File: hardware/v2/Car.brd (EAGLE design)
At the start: 84 x 56 mm, 63 parts

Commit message: Completed Rev.A of v2 hardware.
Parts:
- removed 3.3V: 317EMP, linear:SOT223
- removed ARMS1: MCP23S08, microchip:SO-18W
- removed DIO1: (no value), SparkFun-Connectors:1X10_LOCK
- removed LED1, LED2: (no value), led:CHIP-LED0805
- removed POW: (no value), SparkFun-Connectors:1X02_XTRA_BIG
- added 3V3: 317EMP, linear:SOT223
- added AIO: (no value), SparkFun-Connectors:1X10_LOCK
- added HB, PWR: (no value), led:CHIP-LED0805
- added J1: (no value), con-jack:DCJ0303
- added M.ARMS: MCP23S08, microchip:SO-18W
- moved C2 28.6 mm to (48.3, 23.5), turned to 270 degrees
- moved R14 10.6 mm to (20.3, 39.4), turned to 270 degrees
- moved 5V 9.04 mm to (14.6, 38.1), turned to 180 degrees
- moved C11 8.95 mm to (8.89, 35.6), turned to 90 degrees
- moved R16 7.87 mm to (20.3, 28.6), turned to 270 degrees
- moved C12 7.33 mm to (5.08, 35.6), turned to 90 degrees
- moved R13 5.10 mm to (20.3, 34.3), turned to 270 degrees
- moved R15 4.57 mm to (20.3, 23.5), turned to 270 degrees
- moved C10 4.35 mm to (8.89, 29.2), turned to 270 degrees
- moved C5 3.58 mm to (64.8, 31.1), turned to 90 degrees
- moved RL1 3.54 mm to (5.08, 24.1), turned to 90 degrees
- moved C7 3.26 mm to (60.3, 17.1), turned to 180 degrees
- moved 22RS 3.16 mm to (28.6, 8.89)
- moved 21RS 3.12 mm to (34.3, 8.89)
- moved 12RS 3.04 mm to (28.6, 47.0)
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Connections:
- net +12V: now also 3V3.3, J1.2; no longer 3.3V.3, POW.1
- net +3V3: now also 3V3.4, AIO.1, M.ARMS.18, M.ARMS.4, M.ARMS.5; no longer 3.3V.4, ARMS1.18, ARMS1.4, ARMS1.5, DIO1.1
- net +5V: now also PWR.A; no longer LED2.A
- net GND: now also AIO.10, J1.1, M.ARMS.9; no longer ARMS1.9, DIO1.10, POW.2
- net N$20: now also 3V3.1; no longer 3.3V.1
- net N$23: now also M.ARMS.12; no longer ARMS1.12
- net N$25: now also M.ARMS.2; no longer ARMS1.2
- net N$26: now also M.ARMS.3; no longer ARMS1.3
- net N$29: now also AIO.4; no longer DIO1.4
- net N$32: now also AIO.5; no longer DIO1.5
- net N$36: now also M.ARMS.7; no longer ARMS1.7
- net N$45: now also AIO.2, HB.A; no longer DIO1.2, LED1.A
- net N$46: now also HB.C; no longer LED1.C
- net N$53: now also AIO.3; no longer DIO1.3
- net N$54: now also AIO.7; no longer DIO1.7
- net N$55: now also AIO.8; no longer DIO1.8
- net N$56: now also M.ARMS.13; no longer ARMS1.13
- net N$57: now also AIO.6; no longer DIO1.6
- net N$59: now also AIO.9; no longer DIO1.9
- net N$60: now also M.ARMS.16; no longer ARMS1.16
- net N$61: now also M.ARMS.17; no longer ARMS1.17
- net N$62: now also M.ARMS.10; no longer ARMS1.10
- net N$63: now also M.ARMS.11; no longer ARMS1.11
- net N$65: now also PWR.C; no longer LED2.C
- net N$66: now also M.ARMS.14; no longer ARMS1.14
- net N$67: now also M.ARMS.15; no longer ARMS1.15
- net N$7: now also M.ARMS.1; no longer ARMS1.1
- net VCCIO: now also M.ARMS.6; no longer ARMS1.6
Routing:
- net N$41: track 92.7 -> 42.2 mm, vias 7 -> 2
- net GND: track 419.5 -> 470.0 mm, vias 18 -> 13
- net N$67: track 23.1 -> 60.9 mm, vias 2 -> 4
- net N$62: track 58.1 -> 22.3 mm
- net N$26: track 71.8 -> 107.4 mm, vias 4 -> 7
- net N$22: track 57.2 -> 91.2 mm, vias 2 -> 4
- net N$66: track 39.1 -> 71.3 mm, vias 2 -> 4
- net +5V: track 201.1 -> 171.4 mm, vias 10 -> 8
- net +12V: track 161.3 -> 183.0 mm, vias 6 -> 9
- net N$50: track 27.7 -> 10.1 mm
- net N$2: track 16.6 -> 31.2 mm, vias 1 -> 2
- net N$7: track 79.6 -> 92.4 mm, vias 5 -> 4
- net +3V3: track 230.0 -> 218.4 mm, vias 13 -> 8
- net N$8: track 31.2 -> 20.2 mm
- net N$30: track 61.8 -> 51.2 mm
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- added copper zone on layer 1, net GND
- added copper zone on layer 16, net GND
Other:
- board size 84 x 56 mm -> 83.8 x 55.9 mm
- board text added: "--"
- board text added: "3V3"
- board text removed: "-"
- board text removed: "3.3v"

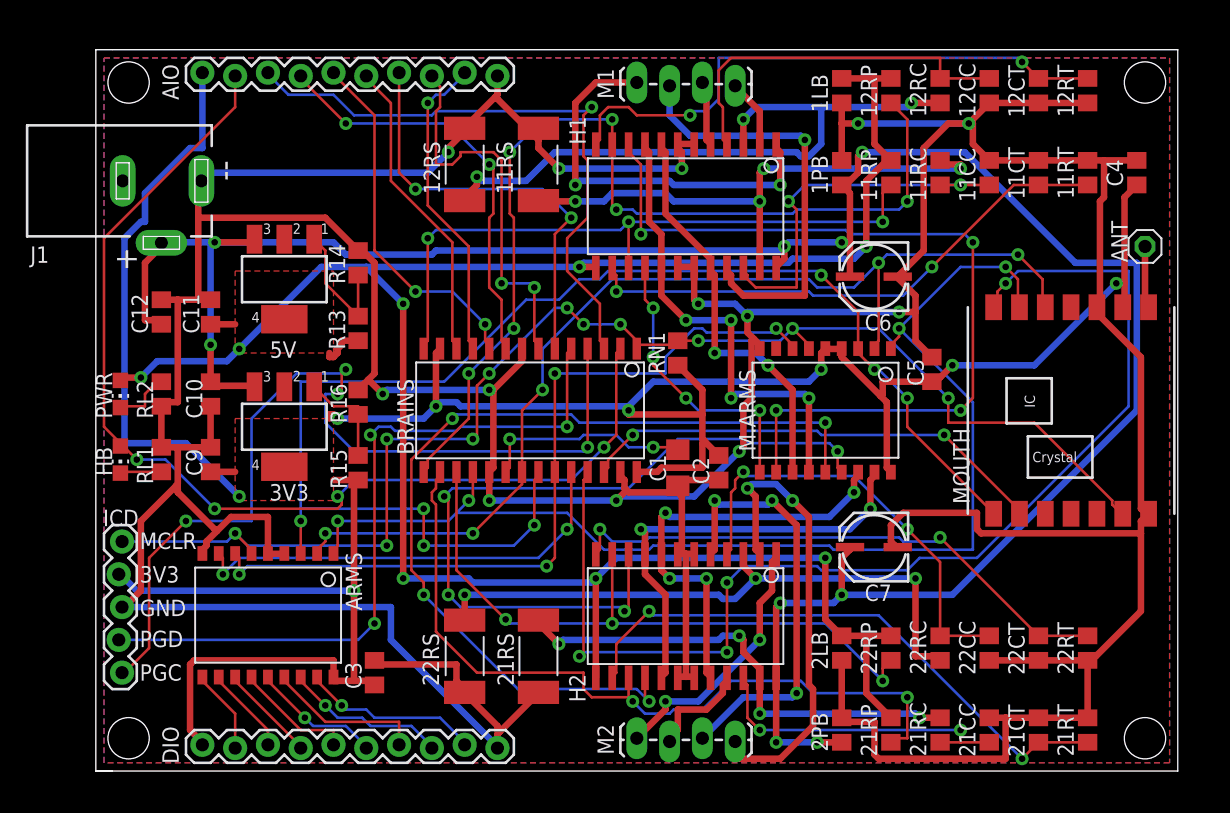
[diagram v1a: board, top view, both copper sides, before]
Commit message: Checkpointing. (about to make so potentially dangerous changes.)
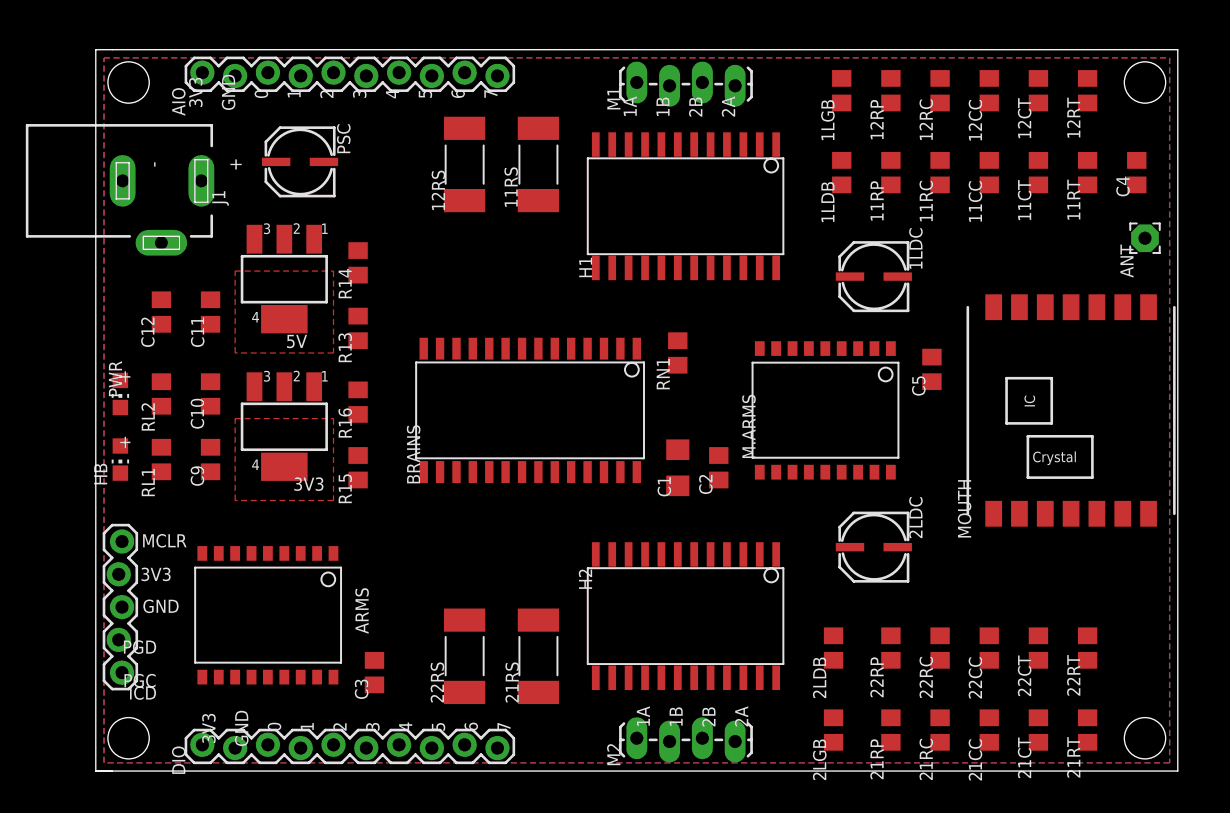
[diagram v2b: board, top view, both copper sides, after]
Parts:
- removed 2LB: 100n, rcl:C0805
- removed 2PB: 100u, rcl:C0805
- added 2LDB, 2LGB: 100n, rcl:C0805
- added PSC: 100u, SparkFun-Passives:PANASONIC_C
- 1LDB: value 100u -> 100n
- 1LDC, 2LDC: value (none) -> 100u
- ANT: device pinhead:1X01 -> wirepad:2,15/1,0
- moved ANT 0.63 mm to (81.3, 41.3), turned to 0 degrees
- renumbered 1LB to 1LGB, 1PB to 1LDB, C6 to 1LDC, C7 to 2LDC
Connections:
- net +12V: now also 2LDB.1, PSC.+; no longer 2PB.1
- net +5V: now also 2LGB.1; no longer 2LB.1
- net GND: now also 2LDB.2, 2LGB.2, PSC.-; no longer 2LB.2, 2PB.2
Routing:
- net GND: track 470.0 -> 0.00 mm, vias 13 -> 0
- net +3V3: track 218.4 -> 0.00 mm, vias 8 -> 0
- net +12V: track 183.0 -> 0.00 mm, vias 9 -> 0
- net +5V: track 171.4 -> 0.00 mm, vias 8 -> 0
- net N$26: track 107.4 -> 0.00 mm, vias 7 -> 0
- net VCCIO: track 107.0 -> 0.00 mm, vias 11 -> 0
- net N$7: track 92.4 -> 0.00 mm, vias 4 -> 0
- net N$22: track 91.2 -> 0.00 mm, vias 4 -> 0
- net N$45: track 84.1 -> 0.00 mm, vias 4 -> 0
- net N$25: track 81.9 -> 0.00 mm, vias 5 -> 0
- net N$21: track 75.1 -> 0.00 mm, vias 6 -> 0
- net N$66: track 71.3 -> 0.00 mm, vias 4 -> 0
- net N$3: track 70.2 -> 0.00 mm, vias 4 -> 0
- net N$63: track 66.1 -> 0.00 mm, vias 4 -> 0
- net N$36: track 62.7 -> 0.00 mm, vias 4 -> 0
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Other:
- board text added: "-"
- board text added: "0"
- board text added: "1"
- board text added: "1A"
- board text added: "1B"
- board text added: "2"
- board text added: "2A"
- board text added: "2B"
- board text added: "3"
- board text added: "4"
- board text added: "5"
- board text added: "6"
- board text added: "7"
- board text removed: "--"

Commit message: Fixed a number of issues discovered from Rev. A boards.
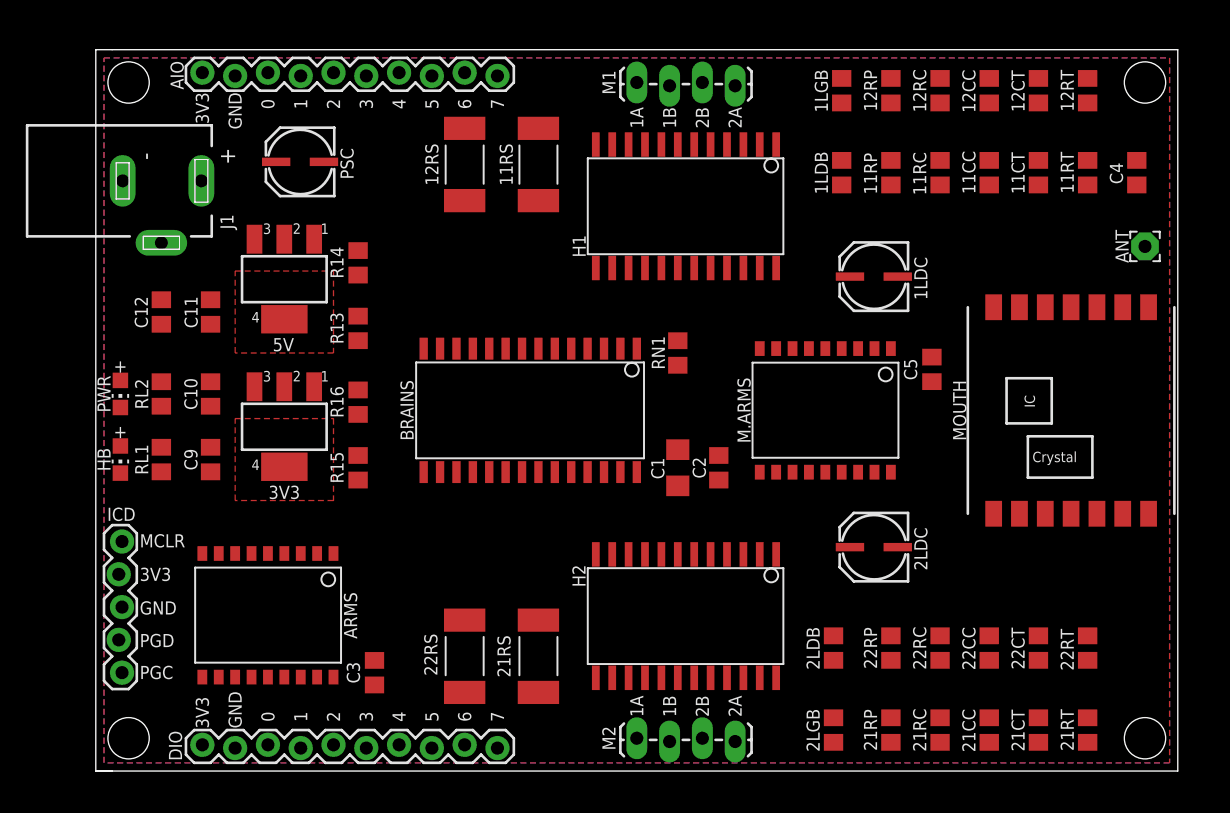
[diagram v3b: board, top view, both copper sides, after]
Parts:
- ANT: value (none) -> ANT
- HB, PWR: value (none) -> LED
- moved ANT 0.63 mm to (81.3, 40.6)
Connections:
- removed net N$51: ARMS.15, DIO.7
- removed net N$52: ARMS.17, DIO.9
- new net N$39: ARMS.11, DIO.4
- new net N$47: ARMS.14, DIO.7
- net +12V: now also J1.1; no longer J1.2
- net GND: now also AIO.2, DIO.2, J1.2; no longer AIO.10, DIO.10, J1.1
- net N$12: now also ARMS.10, DIO.3; no longer ARMS.16, DIO.8
- net N$29: now also AIO.5; no longer AIO.4
- net N$32: now also AIO.6; no longer AIO.5
- net N$43: now also ARMS.12, DIO.5; no longer ARMS.10, DIO.2
- net N$44: now also ARMS.13, DIO.6; no longer ARMS.11, DIO.3
- net N$45: now also AIO.3; no longer AIO.2
- net N$48: now also ARMS.15, DIO.8; no longer ARMS.12, DIO.4
- net N$49: now also ARMS.16, DIO.9; no longer ARMS.13, DIO.5
- net N$50: now also ARMS.17, DIO.10; no longer ARMS.14, DIO.6
- net N$53: now also AIO.4; no longer AIO.3
- net N$54: now also AIO.8; no longer AIO.7
- net N$55: now also AIO.9; no longer AIO.8
- net N$57: now also AIO.7; no longer AIO.6
- net N$59: now also AIO.10; no longer AIO.9

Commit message: Minor cleanup.
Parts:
- PSB2: value 100n -> 1u
- moved 2LDB 0.63 mm to (57.8, 9.53)
- moved 2LGB 0.63 mm to (57.8, 3.17)
- renumbered C10 to PSB3, C12 to PSB2, PSC to PSB1
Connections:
- net GND: now also J1.3; no longer J1.2
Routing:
- removed copper zone on layer 1, net GND
- removed copper zone on layer 16, net GND
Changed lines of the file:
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@@
 <setting verticaltext="up"/>
 </settings>
-<grid distance="25" unitdist="mil" unit="inch" style="lines" multiple="2" display="yes" altdistance="5" altunitdist="mil" altunit="inch"/>
+<grid distance="25" unitdist="mil" unit="mm" style="lines" multiple="1" display="yes" altdistance="5" altunitdist="mil" altunit="mm"/>
 <layers>
 <layer number="1" name="Top" color="4" fill="1" visible="yes" active="yes"/>
@@
 <attribute name="VALUE" x="9.3" y="24.076" size="1.016" layer="27" rot="R90" align="center"/>
 </element>
-<element name="C10" library="rcl" package="C0805" value="100n" x="8.89" y="29.21" smashed="yes" rot="R270">
+<element name="PSB3" library="rcl" package="C0805" value="100n" x="8.89" y="29.21" smashed="yes" rot="R270">
 <attribute name="NAME" x="7.366" y="29.21" size="1.016" layer="25" rot="R90" align="center"/>
 <attribute name="VALUE" x="9.3" y="29.191" size="1.016" layer="27" rot="R90" align="center"/>
@@
 <attribute name="VALUE" x="9.297" y="35.579" size="1.016" layer="27" rot="R90" align="center"/>
 </element>
-<element name="C12" library="rcl" package="C0805" value="100n" x="5.08" y="35.56" smashed="yes" rot="R90">
+<element name="PSB2" library="rcl" package="C0805" value="1u" x="5.08" y="35.56" smashed="yes" rot="R90">
 <attribute name="NAME" x="3.527" y="35.541" size="1.016" layer="25" rot="R90" align="center"/>
 <attribute name="VALUE" x="5.445" y="35.468" size="1.016" layer="27" rot="R90" align="center"/>
@@
 <attribute name="NAME" x="0.635" y="24.13" size="1.016" layer="25" rot="R270" align="center"/>
 </element>
-<element name="2LDB" library="rcl" package="C0805" value="100n" x="57.15" y="9.525" smashed="yes" rot="R270">
-<attribute name="NAME" x="55.572" y="9.506" size="1.016" layer="25" rot="R90" align="center"/>
-<attribute name="VALUE" x="57.509" y="9.55" size="1.016" layer="27" rot="R90" align="center"/>
-</element>
-<element name="2LGB" library="rcl" package="C0805" value="100n" x="57.15" y="3.175" smashed="yes" rot="R90">
-<attribute name="NAME" x="55.572" y="3.156" size="1.016" layer="25" rot="R90" align="center"/>
-<attribute name="VALUE" x="57.563" y="3.073" size="1.016" layer="27" rot="R90" align="center"/>
+<element name="2LDB" library="rcl" package="C0805" value="100n" x="57.785" y="9.525" smashed="yes" rot="R270">
+<attribute name="NAME" x="56.207" y="9.506" size="1.016" layer="25" rot="R90" align="center"/>
+<attribute name="VALUE" x="58.144" y="9.55" size="1.016" layer="27" rot="R90" align="center"/>
+</element>
+<element name="2LGB" library="rcl" package="C0805" value="100n" x="57.785" y="3.175" smashed="yes" rot="R90">
+<attribute name="NAME" x="56.207" y="3.156" size="1.016" layer="25" rot="R90" align="center"/>
+<attribute name="VALUE" x="58.198" y="3.073" size="1.016" layer="27" rot="R90" align="center"/>
 </element>
 <element name="1LGB" library="rcl" package="C0805" value="100n" x="57.785" y="52.705" smashed="yes" rot="R270">
@@
 <attribute name="VALUE" x="81.28" y="41.64" size="0.0254" layer="27"/>
 </element>
-<element name="PSC" library="SparkFun-Passives" package="PANASONIC_C" value="100u" x="15.875" y="46.99" smashed="yes" rot="R180">
+<element name="PSB1" library="SparkFun-Passives" package="PANASONIC_C" value="100u" x="15.875" y="46.99" smashed="yes" rot="R180">
 <attribute name="NAME" x="19.464" y="47.05" size="1.016" layer="25" rot="R270" align="center"/>
 <attribute name="VALUE" x="15.896" y="46.93" size="1.016" layer="27" rot="R90" align="center"/>
@@
 <wire x1="1.905" y1="30.26" x2="8.89" y2="34.61" width="0" layer="19" extent="1-1"/>
 <wire x1="38.736" y1="7.222" x2="38.736" y2="38.972" width="0" layer="19" extent="1-1"/>
-<wire x1="57.15" y1="2.225" x2="38.736" y2="7.222" width="0" layer="19" extent="1-1"/>
-<wire x1="61.595" y1="4.125" x2="57.15" y2="2.225" width="0" layer="19" extent="1-1"/>
+<wire x1="57.785" y1="2.225" x2="38.736" y2="7.222" width="0" layer="19" extent="1-1"/>
+<wire x1="61.595" y1="4.125" x2="57.785" y2="2.225" width="0" layer="19" extent="1-1"/>
 <wire x1="61.595" y1="10.475" x2="61.595" y2="4.125" width="0" layer="19" extent="1-1"/>
 </signal>
@@
 <contactref element="MOUTH" pad="10"/>
 <contactref element="MOUTH" pad="7"/>
-<contactref element="R14" pad="1"/>
-<contactref element="C11" pad="2"/>
 <contactref element="C1" pad="2"/>
 <contactref element="BRAINS" pad="8"/>
 <contactref element="BRAINS" pad="19"/>
 <contactref element="BRAINS" pad="27"/>
-<contactref element="C12" pad="2"/>
-<contactref element="C10" pad="2"/>
 <contactref element="C2" pad="2"/>
 <contactref element="C4" pad="2"/>
@@
 <contactref element="M.ARMS" pad="9"/>
 <contactref element="C5" pad="2"/>
-<contactref element="RL2" pad="2"/>
 <contactref element="1LDC" pad="-"/>
 <contactref element="2LDC" pad="-"/>
-<polygon width="0.4064" layer="1" isolate="0.4064" orphans="yes" rank="6">
-<vertex x="0.635" y="55.245"/>
-<vertex x="83.185" y="55.245"/>
-<vertex x="83.185" y="0.635"/>
-<vertex x="0.635" y="0.635"/>
-</polygon>
-<polygon width="0.4064" layer="16" isolate="0.4064" orphans="yes" rank="6">
-<vertex x="0.635" y="55.245"/>
-<vertex x="83.185" y="55.245"/>
-<vertex x="83.185" y="0.635"/>
-<vertex x="0.635" y="0.635"/>
-</polygon>
-<contactref element="PSC" pad="-"/>
 <contactref element="DIO" pad="2"/>
 <contactref element="AIO" pad="2"/>
-<contactref element="J1" pad="2"/>
+<contactref element="PSB2" pad="2"/>
+<contactref element="PSB1" pad="-"/>
+<contactref element="PSB3" pad="2"/>
+<contactref element="R14" pad="1"/>
+<contactref element="RL2" pad="2"/>
+<contactref element="C11" pad="2"/>
+<contactref element="J1" pad="3"/>
 <wire x1="73.025" y1="51.755" x2="76.835" y2="51.755" width="0" layer="19" extent="1-1"/>
 <wire x1="69.215" y1="51.755" x2="73.025" y2="51.755" width="0" layer="19" extent="1-1"/>
@@
 <wire x1="34.29" y1="49.79" x2="45.086" y2="48.532" width="0" layer="19" extent="1-1"/>
 <wire x1="28.575" y1="49.79" x2="34.29" y2="49.79" width="0" layer="19" extent="1-1"/>
-<wire x1="57.15" y1="8.575" x2="46.356" y2="7.222" width="0" layer="19" extent="1-1"/>
-<wire x1="57.15" y1="4.125" x2="57.15" y2="8.575" width="0" layer="19" extent="1-1"/>
-<wire x1="62.125" y1="17.345" x2="57.15" y2="8.575" width="0" layer="19" extent="1-1"/>
 <wire x1="34.29" y1="6.09" x2="45.086" y2="7.222" width="0" layer="19" extent="1-1"/>
 <wire x1="28.575" y1="6.09" x2="34.29" y2="6.09" width="0" layer="19" extent="1-1"/>
@@
 <wire x1="8.89" y1="36.51" x2="8.89" y2="28.26" width="0" layer="19" extent="1-1"/>
 <wire x1="5.08" y1="36.51" x2="8.89" y2="36.51" width="0" layer="19" extent="1-1"/>
-<wire x1="5.08" y1="40.92" x2="5.08" y2="36.51" width="0" layer="19" extent="1-1"/>
+<wire x1="2.08" y1="45.72" x2="5.08" y2="36.51" width="0" layer="19" extent="1-1"/>
 <wire x1="17.675" y1="47.19" x2="28.575" y2="49.79" width="0" layer="19" extent="1-1"/>
 <wire x1="20.32" y1="40.32" x2="17.675" y2="47.19" width="0" layer="19" extent="1-1"/>
 <wire x1="10.795" y1="53.848" x2="17.675" y2="47.19" width="0" layer="19" extent="1-1"/>
 <wire x1="20.32" y1="29.525" x2="20.32" y2="40.32" width="0" layer="19" extent="1-1"/>
+<wire x1="57.785" y1="8.575" x2="46.356" y2="7.222" width="0" layer="19" extent="1-1"/>
+<wire x1="57.785" y1="4.125" x2="57.785" y2="8.575" width="0" layer="19" extent="1-1"/>
+<wire x1="62.125" y1="17.345" x2="57.785" y2="8.575" width="0" layer="19" extent="1-1"/>
 <wire x1="69.215" y1="8.575" x2="62.125" y2="17.345" width="0" layer="19" extent="1-1"/>
 <wire x1="73.025" y1="8.575" x2="69.215" y2="8.575" width="0" layer="19" extent="1-1"/>
@@
 </signal>
 <signal name="+12V" class="1">
-<contactref element="5V" pad="3"/>
-<contactref element="3V3" pad="3"/>
 <contactref element="H1" pad="24"/>
 <contactref element="1LDB" pad="1"/>
 <contactref element="H2" pad="24"/>
 <contactref element="2LDB" pad="1"/>
-<contactref element="C12" pad="1"/>
-<contactref element="C10" pad="1"/>
 <contactref element="1LDC" pad="+"/>
 <contactref element="2LDC" pad="+"/>
-<contactref element="PSC" pad="+"/>
+<contactref element="PSB1" pad="+"/>
 <contactref element="J1" pad="1"/>
+<contactref element="5V" pad="3"/>
+<contactref element="PSB2" pad="1"/>
+<contactref element="3V3" pad="3"/>
+<contactref element="PSB3" pad="1"/>
 <wire x1="58.425" y1="38.3" x2="57.785" y2="45.405" width="0" layer="19" extent="1-1"/>
 <wire x1="52.706" y1="38.972" x2="58.425" y2="38.3" width="0" layer="19" extent="1-1"/>
 <wire x1="58.425" y1="17.345" x2="58.425" y2="38.3" width="0" layer="19" extent="1-1"/>
-<wire x1="57.15" y1="10.475" x2="58.425" y2="17.345" width="0" layer="19" extent="1-1"/>
-<wire x1="52.706" y1="7.222" x2="57.15" y2="10.475" width="0" layer="19" extent="1-1"/>
+<wire x1="57.785" y1="10.475" x2="58.425" y2="17.345" width="0" layer="19" extent="1-1"/>
+<wire x1="52.706" y1="7.222" x2="57.785" y2="10.475" width="0" layer="19" extent="1-1"/>
 <wire x1="13.975" y1="47.19" x2="52.706" y2="38.972" width="0" layer="19" extent="1-1"/>
 <wire x1="8.18" y1="45.72" x2="13.975" y2="47.19" width="0" layer="19" extent="1-1"/>
